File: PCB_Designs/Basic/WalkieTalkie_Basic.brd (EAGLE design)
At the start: 33 x 50.8 mm, 61 parts, among them IC1 AD8609RU, IC2 AD8603UJ, IC3 MCP601OT, Q1 MOSFET-NCHANNELBSS123LT1G

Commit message: updates. almost done
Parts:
- added U$4: PS1240P02CT3P, Orlando:PIEZO-1
- turned LIPO to 90 degrees
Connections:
- net GND: now also LIPO.P$2; no longer LIPO.P$1
- net V_BATT: now also LIPO.P$1; no longer LIPO.P$2
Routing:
- net V_BATT: track 7.08 -> 5.76 mm

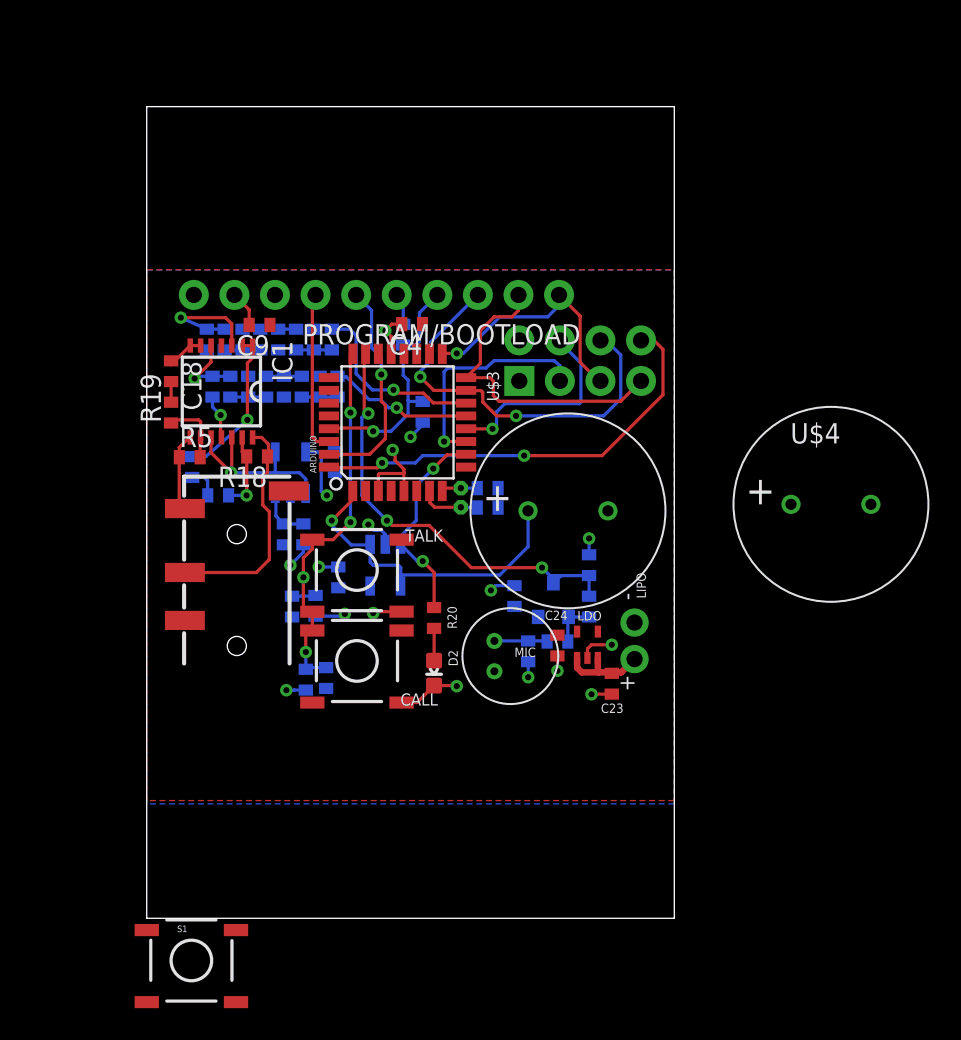
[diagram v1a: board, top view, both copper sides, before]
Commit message: finished board design. sent to fab (OSH Park)
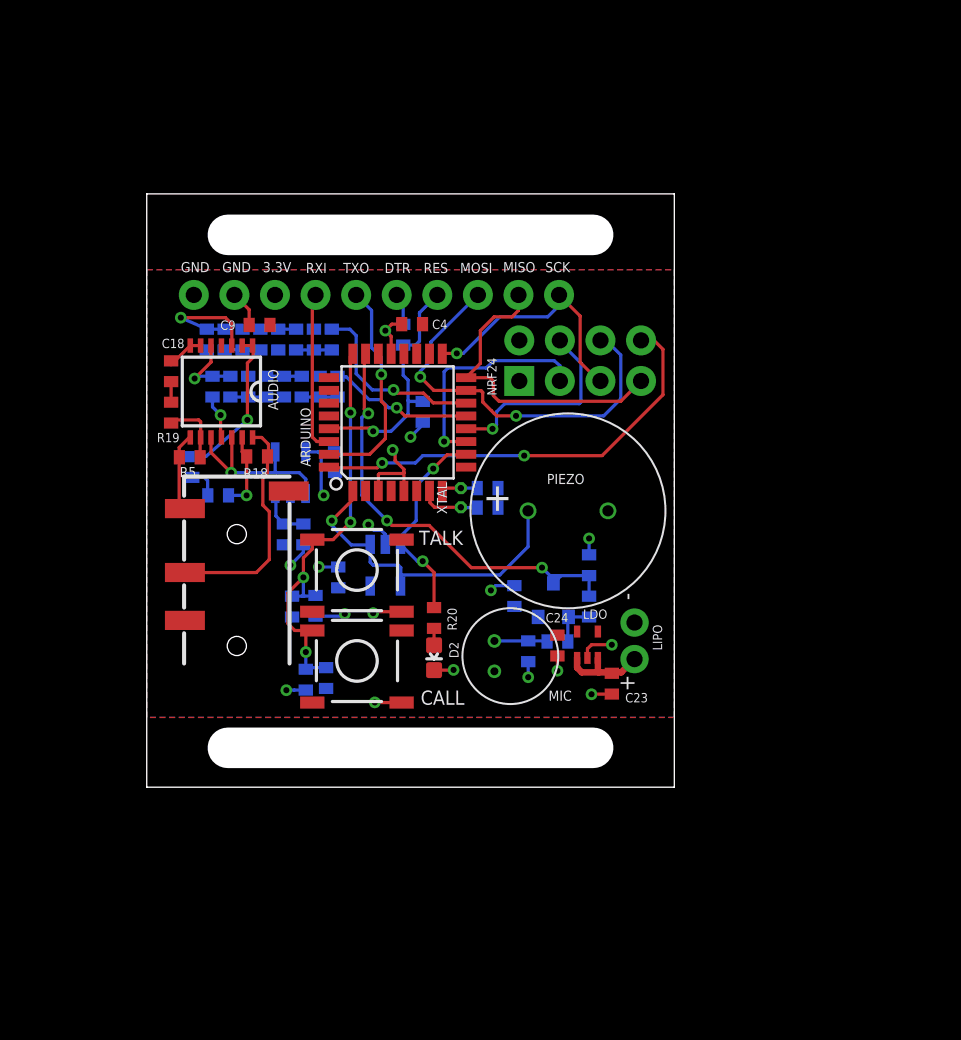
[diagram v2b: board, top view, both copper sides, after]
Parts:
- removed S1: TAC_SWITCHSMD, SparkFun-Retired:TACTILE-SWITCH-SMD
- removed U$4: PS1240P02CT3P, Orlando:PIEZO-1
- moved D2 0.97 mm to (18.0, 16.4)
- renumbered IC1 to AUDIO, IC2 to VREF, PROGRAM/BOOTLOAD to PROGRAM/BOOTLOADING, Q1 to MIC-AMP, U$3 to NRF24
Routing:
- net TALK/CALL: track 26.2 -> 27.7 mm
- net GND: track 23.7 -> 22.6 mm, vias 8 -> 9
- net N$6: track 2.03 -> 1.06 mm
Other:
- board size 33 x 50.8 mm -> 33 x 37.1 mm
- board text added: "3.3V"
- board text added: "CUT-OUT"
- board text added: "DTR"
- board text added: "GND"
- board text added: "MISO"
- board text added: "MOSI"
- board text added: "OS Hoilett IICEPD, CalvaryEng Walkie Talkie"
- board text added: "PIEZO"
- board text added: "RES"
- board text added: "RXI"
- board text added: "SCK"
- board text added: "TXO"
- board text added: "XTAL"

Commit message: updated pcb files with comments, labels, etc
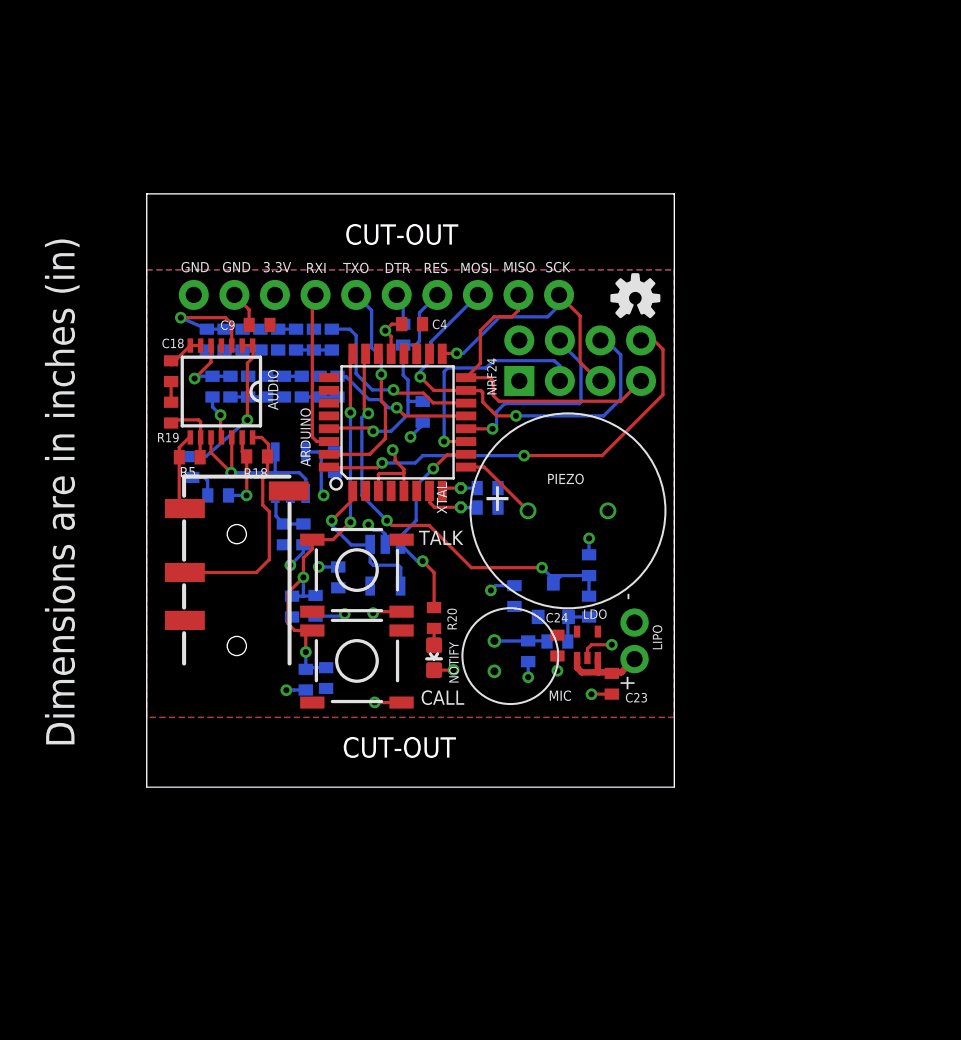
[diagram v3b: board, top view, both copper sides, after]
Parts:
- added LOGO1: OSHW-LOGOS, SparkFun-Aesthetics:OSHW-LOGO-S
- renumbered D2 to NOTIFY
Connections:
- net D3: no longer U$2.+
- net D5: now also U$2.+
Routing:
- net D3: track 20.9 -> 9.96 mm
- net D5: track 0.00 -> 5.01 mm
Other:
- outline, holes or cut-outs redrawn
- board text added: "Dimensions are in inches (in)"
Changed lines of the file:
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@@
 <setting verticaltext="up"/>
 </settings>
-<grid distance="4" unitdist="mil" unit="mil" style="lines" multiple="1" display="yes" altdistance="0.025" altunitdist="inch" altunit="inch"/>
+<grid distance="2" unitdist="mil" unit="mil" style="lines" multiple="1" display="yes" altdistance="0.025" altunitdist="inch" altunit="inch"/>
 <layers>
 <layer number="1" name="Top" color="4" fill="1" visible="yes" active="yes"/>
@@
 <board>
 <plain>
-<wire x1="0" y1="8.2042" x2="33.02" y2="8.2042" width="0" layer="20"/>
+<wire x1="0" y1="8.2042" x2="33.02" y2="8.2042" width="0" layer="21"/>
 <wire x1="33.02" y1="8.2042" x2="33.02" y2="45.339" width="0" layer="20"/>
 <wire x1="33.02" y1="45.339" x2="0" y2="45.339" width="0" layer="20"/>
@@
 <text x="25.0444" y="27.178" size="0.635" layer="25">PIEZO</text>
 <text x="18.796" y="25.2984" size="0.635" layer="25" rot="R90">XTAL</text>
-<wire x1="5.08" y1="10.668" x2="27.94" y2="10.668" width="2.54" layer="20"/>
-<wire x1="5.08" y1="42.7736" x2="27.94" y2="42.7736" width="2.54" layer="20"/>
+<wire x1="5.08" y1="10.668" x2="27.94" y2="10.668" width="2.54" layer="50"/>
+<wire x1="5.08" y1="42.7736" x2="27.94" y2="42.7736" width="2.54" layer="50"/>
 <text x="12.3952" y="42.164" size="1.27" layer="20">CUT-OUT</text>
-<text x="12.0904" y="10.2616" size="1.27" layer="20">CUT-OUT</text>
+<text x="12.2428" y="10.0584" size="1.27" layer="20">CUT-OUT</text>
+<dimension x1="0" y1="8.2042" x2="33.02" y2="8.2042" x3="16.51" y3="5.4864" textsize="1.778" layer="21" unit="inch"/>
+<dimension x1="0" y1="12.573" x2="0" y2="40.5892" x3="-1.4224" y3="26.5811" textsize="1.778" layer="21" unit="inch"/>
+<dimension x1="33.02" y1="8.2042" x2="33.02" y2="45.339" x3="36.068" y3="26.7716" textsize="1.778" layer="21" unit="inch"/>
+<text x="-4.5212" y="10.668" size="1.778" layer="21" rot="R90">Dimensions are in inches (in)</text>
 </plain>
 <attributes>
@@
 <attribute name="NAME" x="21.8948" y="32.7152" size="0.5842" layer="25" rot="R90"/>
 </element>
-<element name="D2" library="SparkFun-LED" package="LED-0603" value="RED" x="17.9832" y="16.4084" smashed="yes" rot="R180">
+<element name="NOTIFY" library="SparkFun-LED" package="LED-0603" value="RED" x="17.9832" y="16.4084" smashed="yes" rot="R180">
 <attribute name="PROD_ID" value="DIO-00819" x="17.9832" y="16.4084" size="1.778" layer="27" rot="R180" display="off"/>
 <attribute name="NAME" x="18.9357" y="17.2974" size="0.5842" layer="25" rot="R270"/>
@@
 <attribute name="VALUE" x="17.2466" y="39.0906" size="1.27" layer="27" rot="R180"/>
 </element>
+<element name="LOGO1" library="SparkFun-Aesthetics" package="OSHW-LOGO-S" value="OSHW-LOGOS" x="30.5816" y="38.8112"/>
 </elements>
 <signals>
@@
 <contactref element="PROGRAM/BOOTLOADING" pad="10"/>
 <contactref element="U$2" pad="-"/>
-<contactref element="D2" pad="C"/>
+<contactref element="NOTIFY" pad="C"/>
 <contactref element="MIC" pad="-"/>
 <polygon width="0.2032" layer="16" isolate="0.2032">
@@
 <signal name="D5">
 <contactref element="ARDUINO" pad="9"/>
+<contactref element="U$2" pad="+"/>
+<wire x1="19.9898" y1="28.2388" x2="21.128" y2="28.2388" width="0.2032" layer="1"/>
+<wire x1="21.128" y1="28.2388" x2="23.8652" y2="25.5016" width="0.2032" layer="1"/>
 </signal>
 <signal name="D4">
@@
 <contactref element="IC3" pad="1"/>
 <contactref element="IC3" pad="4"/>
-<contactref element="U$2" pad="+"/>
 <wire x1="13.9852" y1="23.404" x2="13.9852" y2="22.286" width="0.2032" layer="16"/>
 <wire x1="13.9852" y1="22.286" x2="14.1732" y2="22.098" width="0.2032" layer="16"/>
 <wire x1="14.1732" y1="22.098" x2="15.748" y2="22.098" width="0.2032" layer="16"/>
 <wire x1="15.748" y1="22.098" x2="15.9004" y2="21.9456" width="0.2032" layer="16"/>
-<wire x1="15.9004" y1="21.9456" x2="15.9004" y2="21.4884" width="0.2032" layer="16"/>
-<wire x1="15.9004" y1="21.4884" x2="15.9004" y2="20.8072" width="0.2032" layer="16"/>
+<wire x1="15.9004" y1="21.9456" x2="15.9004" y2="20.8072" width="0.2032" layer="16"/>
 <wire x1="15.9004" y1="20.8072" x2="15.8852" y2="20.792" width="0.2032" layer="16"/>
-<wire x1="23.8652" y1="25.5016" x2="23.8652" y2="23.2556" width="0.2032" layer="16"/>
-<wire x1="23.8652" y1="23.2556" x2="22.098" y2="21.4884" width="0.2032" layer="16"/>
-<wire x1="22.098" y1="21.4884" x2="15.9004" y2="21.4884" width="0.2032" layer="16"/>
 <wire x1="12.8972" y1="26.7462" x2="12.8972" y2="26.2068" width="0.2032" layer="1"/>
 <wire x1="12.8972" y1="26.2068" x2="11.5824" y2="24.892" width="0.2032" layer="1"/>
@@
 </signal>
 <signal name="N$6">
-<contactref element="D2" pad="A"/>
+<contactref element="NOTIFY" pad="A"/>
 <contactref element="R20" pad="1"/>
 <wire x1="17.9832" y1="18.146" x2="17.9832" y2="17.0854" width="0.2032" layer="1"/>
